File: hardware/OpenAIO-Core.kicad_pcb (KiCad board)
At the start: 6 copper layers, 23 x 20.1 mm, 91 parts, among them J23 SCL, J26 SDA, J30 5V, J34 GND, J35 GND, J37 5V, J38 CAM, J39 VTX, J40 GND, J42 4V5, J43 GND, J44 PIO_TX0, J45 PIO_RX0, J48 RX0, J49 TX0, J50 GND, J52 4V5, J53 GND, J54 TX1, J55 RX1, J91 Core_LGA, Q1 AP1606, Q2 AP1606, U1 TS2306A 240GF MSM 9_C2976675, U10 COS8051SOT, U11 TLV7031DPWR, U2 RP2354A, U6 LP5912-1.8DRVR, U7 LP5912-3.3DRVR, U8 BMI270, U9 SN74LVC1G3157DTBR, X1 XTM25012000JT00351001

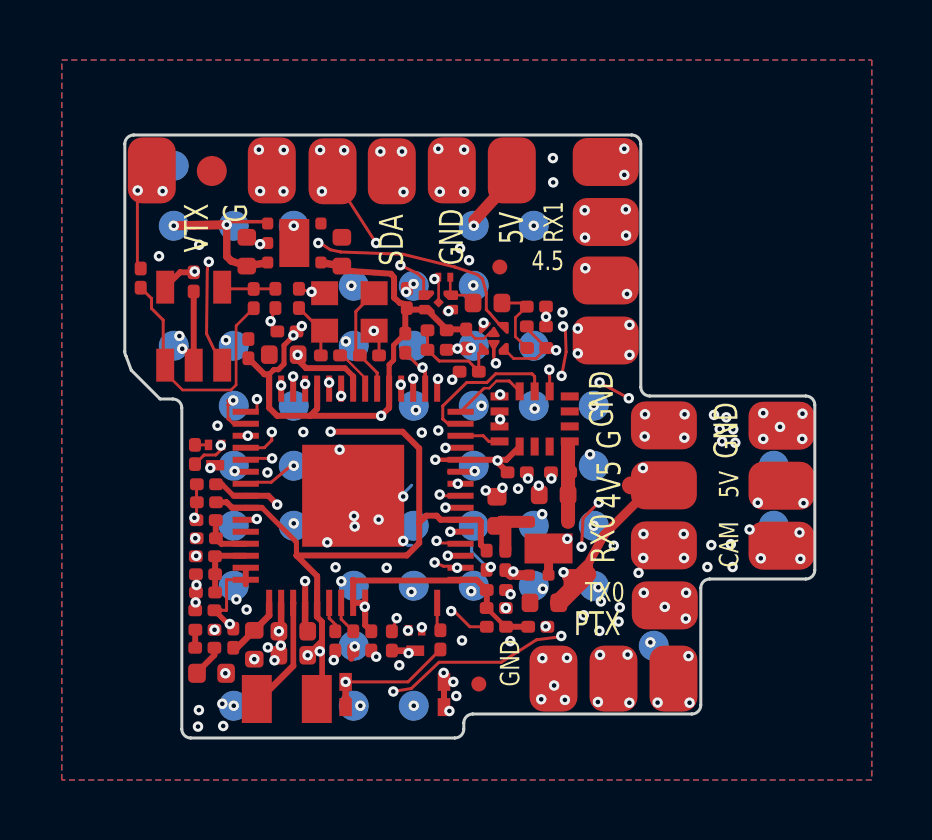
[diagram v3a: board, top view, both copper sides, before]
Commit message: Silk: board identity, forward arrow, motor map, title blocks (FB5 item 3, V5/M4)
- Core B.Silk: OpenDrone mark + "OpenAIO Core / r2 2026-10" (stroke font 0.65)
  and a forward arrow, clear of the J91 pads. Core top has no free area.
- Base B.Silk: "OpenAIO Base / r2 2026-10" (vertical) + OpenDrone mark in the
  old motor-map area; motor map M1-M4 moved to Base F.Silk with a forward arrow.
- Forward = SH-6 (U12) edge, matches config.h GYRO_1_ALIGN CW180_DEG (I8).
- Core F: TX0 now alone beside J44; J49 PTX moved to the README legend
  (the J44/J49 corner has room for one unambiguous label only).
- Title blocks filled (title, rev r2, date 2026-10, LGA R2a pairing).
- Removed the Cmts.User 'TODO brand mark' text.
DRC unchanged (Base 39, Core 28), parity unchanged, unconnected 0/0, copper identical.

Co-Authored-By: Claude Opus 5.5 <noreply@anthropic.com>
Claude-Session: https://claude.ai/code/session_01KTp3FLjVXfXdWrkmr6af7d
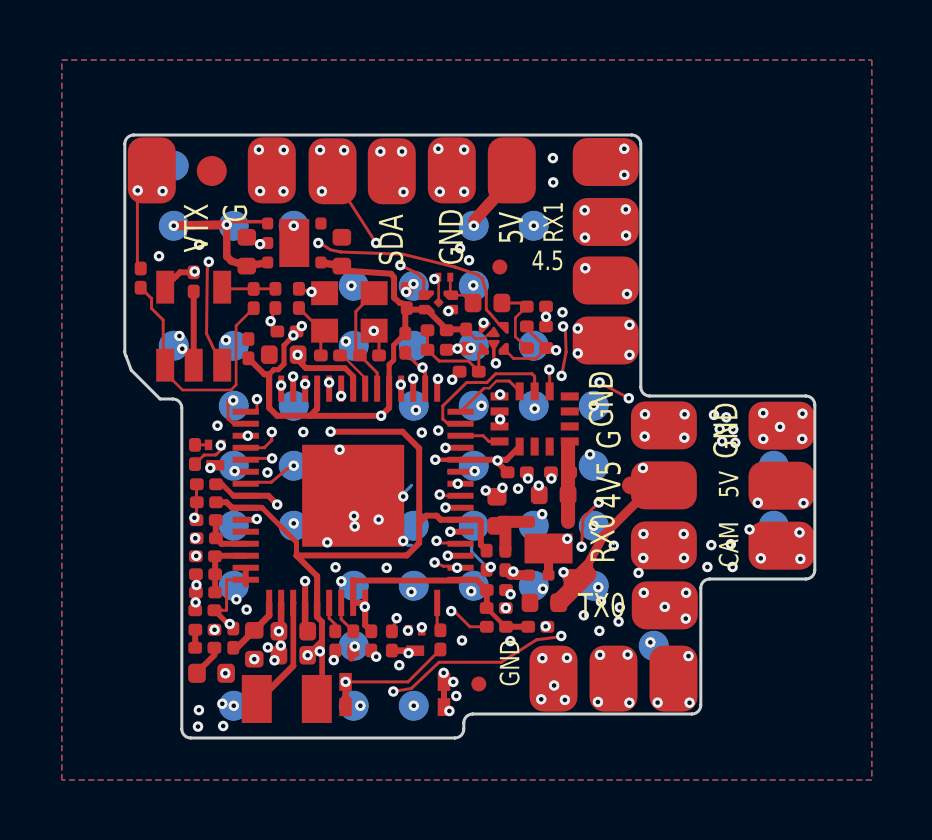
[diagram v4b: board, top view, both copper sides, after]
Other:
- board text added: "OpenAIO Core"
- board text added: "r2 2026-10"
- board text removed: "PTX"
- board text removed: "TODO brand mark: incutec wordmark from the brand repo (not in R1)"
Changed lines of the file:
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@@
 	)
 	(paper "A4")
+	(title_block
+		(title "OpenAIO Core")
+		(date "2026-10")
+		(rev "r2")
+		(comment 1 "LGA interface R2a (46 pads, J91 on B.Cu); pairs with OpenAIO Base r2")
+		(comment 2 "Forward = SH-6 (U12) edge of the Base, arrow on B.Silk (config.h GYRO_1_ALIGN CW180_DEG)")
+		(comment 3 "Fab + assembly: NextPCB")
+	)
 	(layers
 		(0 "F.Cu" signal)
@@
 		(embedded_fonts no)
 	)
+	(gr_poly
+		(pts
+			(xy 113.1 47.1) (xy 113.399999 47.1) (xy 112.949999 47.8) (xy 112.499999 47.1) (xy 112.799999 47.1)
+			(xy 112.799999 46.2) (xy 113.1 46.2)
+		)
+		(stroke
+			(width 0)
+			(type default)
+		)
+		(fill yes)
+		(layer "B.SilkS")
+	)
+	(gr_poly
+		(pts
+			(xy 115.690958 44.103936) (xy 115.73086 44.105734) (xy 115.770246 44.108994) (xy 115.863263 44.123102)
+			(xy 115.951504 44.145527) (xy 116.034678 44.17601) (xy 116.112499 44.21429) (xy 116.184677 44.260109)
+			(xy 116.250923 44.313208) (xy 116.310948 44.373327) (xy 116.364464 44.440207) (xy 116.411182 44.51359)
+			(xy 116.450812 44.593215) (xy 116.483067 44.678824) (xy 116.507657 44.770157) (xy 116.513018 44.795247)
+			(xy 116.517669 44.81834) (xy 116.521653 44.839947) (xy 116.525015 44.860583) (xy 116.5278 44.88076)
+			(xy 116.530051 44.90099) (xy 116.531813 44.921787) (xy 116.533132 44.943663) (xy 116.53405 44.967131)
+			(xy 116.534613 44.992705) (xy 116.534865 45.020896) (xy 116.53485 45.052218) (xy 116.534687 45.085585)
+			(xy 116.534171 45.116362) (xy 116.533258 45.144935) (xy 116.531907 45.171693) (xy 116.530075 45.197021)
+			(xy 116.527718 45.221307) (xy 116.524795 45.244938) (xy 116.521263 45.2683) (xy 116.517079 45.291781)
+			(xy 116.512201 45.315767) (xy 116.506586 45.340646) (xy 116.500192 45.366803) (xy 116.477176 45.443472)
+			(xy 116.448521 45.516049) (xy 116.414431 45.584331) (xy 116.375108 45.648114) (xy 116.330757 45.707194)
+			(xy 116.281582 45.761368) (xy 116.227785 45.810433) (xy 116.169571 45.854184) (xy 116.107143 45.892418)
+			(xy 116.040705 45.924931) (xy 115.970461 45.95152) (xy 115.896614 45.971981) (xy 115.870033 45.977409)
+			(xy 115.840994 45.98221) (xy 115.80997 45.986361) (xy 115.777435 45.989833) (xy 115.743863 45.992602)
+			(xy 115.709729 45.994642) (xy 115.675505 45.995926) (xy 115.641667 45.996429) (xy 115.608688 45.996125)
+			(xy 115.577042 45.994987) (xy 115.547203 45.992991) (xy 115.519644 45.99011) (xy 115.417227 45.972052)
+			(xy 115.3213 45.9442) (xy 115.232135 45.906848) (xy 115.150001 45.860286) (xy 115.075169 45.804809)
+			(xy 115.007909 45.740707) (xy 114.948492 45.668275) (xy 114.897187 45.587803) (xy 114.854265 45.499586)
+			(xy 114.819997 45.403915) (xy 114.794652 45.301083) (xy 114.778502 45.191382) (xy 114.775866 45.158801)
+			(xy 114.774081 45.124508) (xy 114.773266 45.094042) (xy 115.163906 45.094042) (xy 115.169895 45.171846)
+			(xy 115.18179 45.245318) (xy 115.199411 45.314135) (xy 115.222578 45.377976) (xy 115.251113 45.436519)
+			(xy 115.284836 45.48944) (xy 115.323566 45.536419) (xy 115.367125 45.577133) (xy 115.415333 45.611259)
+			(xy 115.46801 45.638476) (xy 115.524976 45.658462) (xy 115.540616 45.661861) (xy 115.559629 45.664596)
+			(xy 115.581345 45.666668) (xy 115.605094 45.668079) (xy 115.630205 45.668831) (xy 115.656009 45.668926)
+			(xy 115.681835 45.668365) (xy 115.707013 45.667151) (xy 115.730873 45.665285) (xy 115.752745 45.662769)
+			(xy 115.771958 45.659605) (xy 115.787842 45.655796) (xy 115.790623 45.65498) (xy 115.793394 45.654148)
+			(xy 115.796156 45.6533) (xy 115.798909 45.652435) (xy 115.801653 45.651553) (xy 115.804388 45.650655)
+			(xy 115.807113 45.649741) (xy 115.809828 45.64881) (xy 115.812535 45.647863) (xy 115.815232 45.6469)
+			(xy 115.817919 45.64592) (xy 115.820597 45.644924) (xy 115.820597 44.45722) (xy 115.814357 44.455017)
+			(xy 115.80806 44.45289) (xy 115.801706 44.450839) (xy 115.795295 44.448866) (xy 115.788829 44.446969)
+			(xy 115.782306 44.445148) (xy 115.775726 44.443405) (xy 115.769091 44.441738) (xy 115.762399 44.440149)
+			(xy 115.755651 44.438636) (xy 115.748847 44.437201) (xy 115.741987 44.435843) (xy 115.727628 44.433608)
+			(xy 115.711447 44.431957) (xy 115.693799 44.430877) (xy 115.675041 44.430353) (xy 115.655528 44.430369)
+			(xy 115.635614 44.430911) (xy 115.615657 44.431964) (xy 115.59601 44.433513) (xy 115.577029 44.435543)
+			(xy 115.559071 44.43804) (xy 115.54249 44.440988) (xy 115.527642 44.444374) (xy 115.474564 44.461616)
+			(xy 115.425244 44.484956) (xy 115.379797 44.514206) (xy 115.338338 44.549177) (xy 115.300981 44.589679)
+			(xy 115.267842 44.635525) (xy 115.239036 44.686525) (xy 115.214676 44.74249) (xy 115.194878 44.803232)
+			(xy 115.179756 44.868561) (xy 115.169426 44.93829) (xy 115.164002 45.012228) (xy 115.163906 45.094042)
+			(xy 114.773266 45.094042) (xy 114.773128 45.0889) (xy 114.772992 45.052376) (xy 114.773656 45.015333)
+			(xy 114.775102 44.97817) (xy 114.777316 44.941285) (xy 114.780279 44.905075) (xy 114.783975 44.869939)
+			(xy 114.788388 44.836276) (xy 114.793501 44.804482) (xy 114.799296 44.774956) (xy 114.818003 44.702568)
+			(xy 114.84151 44.633478) (xy 114.869686 44.567851) (xy 114.902401 44.50585) (xy 114.939521 44.44764)
+			(xy 114.980916 44.393387) (xy 115.026455 44.343255) (xy 115.076005 44.297409) (xy 115.129436 44.256014)
+			(xy 115.186616 44.219234) (xy 115.247414 44.187235) (xy 115.311698 44.16018) (xy 115.344731 44.148899)
+			(xy 115.379433 44.138801) (xy 115.415588 44.129913) (xy 115.452975 44.122264) (xy 115.491377 44.115882)
+			(xy 115.530575 44.110793) (xy 115.57035 44.107027) (xy 115.610485 44.10461) (xy 115.650761 44.10357)
+		)
+		(stroke
+			(width 0)
+			(type default)
+		)
+		(fill yes)
+		(layer "B.SilkS")
+	)
 	(gr_line
 		(start 103.1 43.8)
@@
 		)
 	)
-	(gr_text "TX0"
-		(at 119.1 58.75 0)
-		(layer "F.SilkS")
-		(effects
-			(font
-				(size 0.65 0.5)
-				(thickness 0.1)
-			)
-		)
-	)
 	(gr_text "GND"
 		(at 115.949999 61.1 90)
@@
 		)
 	)
-	(gr_text "PTX"
-		(at 118.85 59.8 0)
+	(gr_text "TX0"
+		(at 118.999999 59.199999 0)
 		(layer "F.SilkS")
 		(effects
@@
 		)
 	)
-	(gr_text "TODO brand mark: incutec wordmark from the brand repo (not in R1)"
-		(at 109.9 47.9 0)
-		(layer "Cmts.User")
+	(gr_text "OpenAIO Core"
+		(at 111.949999 44.585 0)
+		(layer "B.SilkS")
 		(effects
 			(font
-				(size 0.5 0.5)
-				(thickness 0.07)
+				(size 0.65 0.5)
+				(thickness 0.1)
+			)
+			(justify mirror)
+		)
+	)
+	(gr_text "r2 2026-10"
+		(at 111.949999 45.62143 0)
+		(layer "B.SilkS")
+		(effects
+			(font
+				(size 0.65 0.5)
+				(thickness 0.1)
 			)
+			(justify mirror)
 		)
 	)
